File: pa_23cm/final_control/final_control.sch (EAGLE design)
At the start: 12 parts, among them IC1 MAX488CSA, IC2 7812T, IC3 7805T, J1 1X2-3.5MM

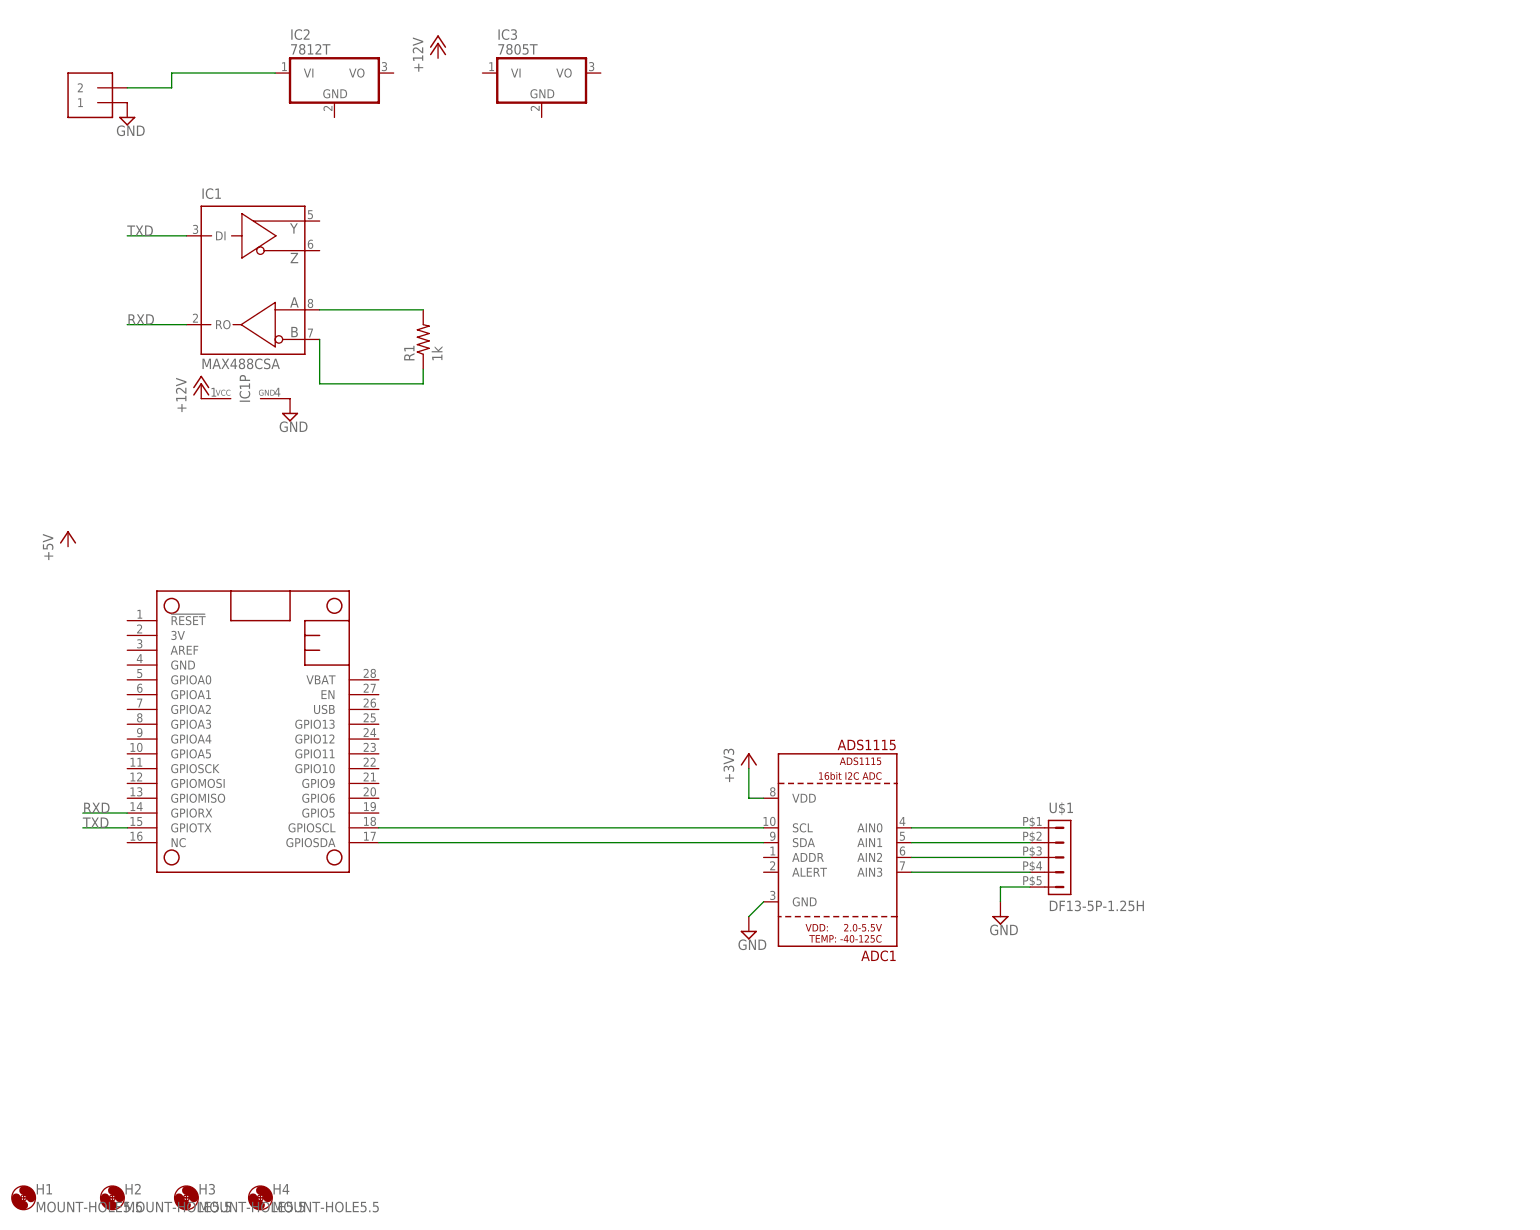
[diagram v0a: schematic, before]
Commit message: aded DECOTEC enclosure parts to library.  Updates to final control board.
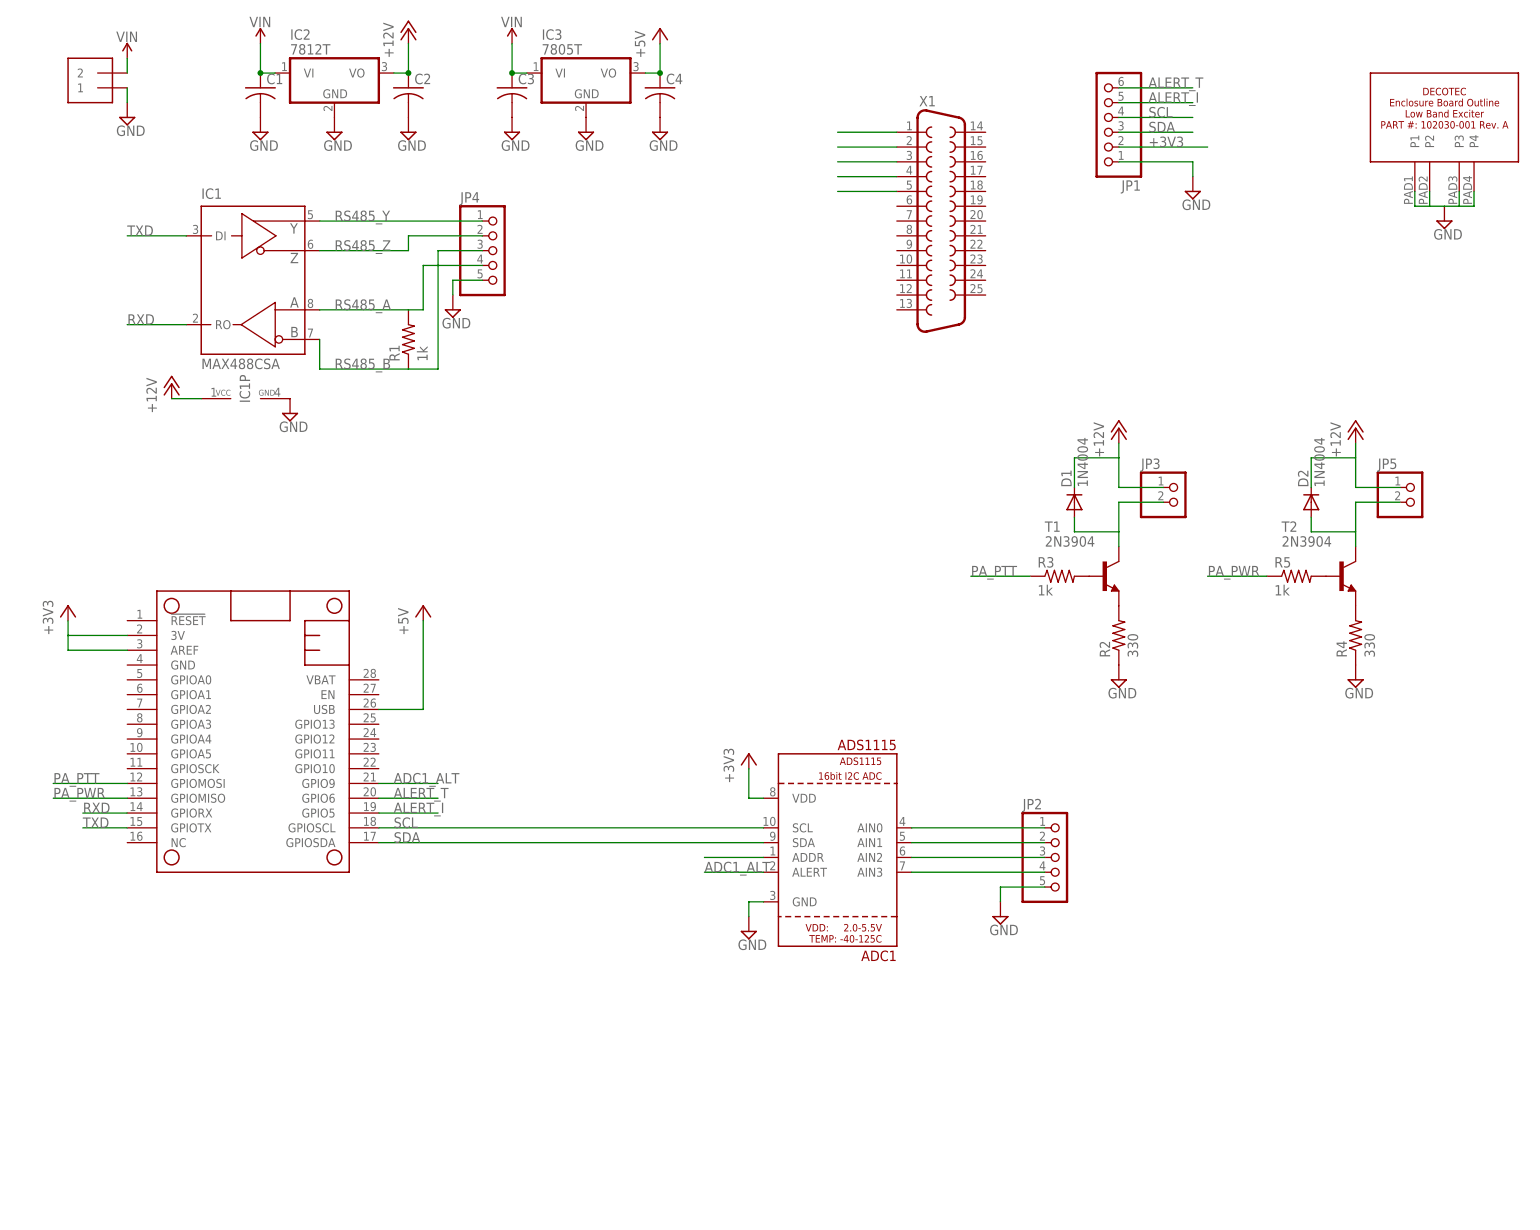
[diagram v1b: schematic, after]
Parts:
- removed H1, H2, H3, H4: MOUNT-HOLE5.5, holes:MOUNT-HOLE5.5
- removed U$1: DF13-5P-1.25H, con-hirose-df13:DF13-5P-1.25H
- added C1, C2, C3, C4: (no value), rcl:C-USC1206K
- added D1, D2: 1N4004, diode:1N4004
- added JP1: (no value), pinhead:PINHD-1X6
- added JP2, JP4: (no value), pinhead:PINHD-1X5
- added JP3, JP5: (no value), pinhead:PINHD-1X2
- added R2, R4: 330, resistor:R-US_R0805
- added R3, R5: 1k, resistor:R-US_R0805
- added T1, T2: 2N3904, transistor:2N3904
- added U$2: DECOTEC_102030-001A, vtgs:DECOTEC_102030-001A
- added X1: (no value), SparkFun-Retired:DB25_FEMALEV
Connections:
- new net +5V: C4.1, FEATHER_32U4.USB, IC3.VO
- new net ADC1_ALT: ADC1.ALERT, FEATHER_32U4.GPIO9
- new net ALERT_I: FEATHER_32U4.GPIO5, JP1.5
- new net ALERT_T: FEATHER_32U4.GPIO6, JP1.6
- new net N$10: R2.2, T1.E
- new net N$11: R3.2, T1.B
- new net N$12: X1.1
- new net N$13: X1.2
- new net N$14: X1.3
- new net N$15: X1.4
- new net N$16: X1.5
- new net PA_PTT: FEATHER_32U4.GPIOMOSI, R3.1
- new net PA_PWR: FEATHER_32U4.GPIOMISO, R5.1
- new net RS485_A: IC1G$1.A, JP4.4, R1.2
- new net RS485_B: IC1G$1.B, JP4.3, R1.1
- new net RS485_Y: IC1G$1.Y, JP4.1
- new net RS485_Z: IC1G$1.Z, JP4.2
- new net SCL: ADC1.SCL, FEATHER_32U4.GPIOSCL, JP1.4
- new net SDA: ADC1.SDA, FEATHER_32U4.GPIOSDA, JP1.3
- new net VIN: C1.1, C3.1, IC2.VI, IC3.VI, J1.2
- net +12V: now also C2.1, D1.C, D2.C, IC2.VO, JP3.1, JP5.1
- net +3V3: now also FEATHER_32U4.3V, FEATHER_32U4.AREF, JP1.2
- net GND: now also C1.2, C2.2, C3.2, C4.2, IC2.GND, IC3.GND, JP1.1, JP2.5, JP4.5, R2.1, R4.1, U$2.P1, U$2.P2, U$2.P3, U$2.P4; no longer U$1.5
- net N$1: now also ADC1.ADDR; no longer IC1G$1.A, R1.2
- net N$2: now also D2.A, JP5.2, T2.C; no longer IC1G$1.B, R1.1
- net N$3: now also R4.2, T2.E; no longer ADC1.SCL, FEATHER_32U4.GPIOSCL
- net N$4: now also R5.2, T2.B; no longer ADC1.SDA, FEATHER_32U4.GPIOSDA
- net N$5: now also JP2.1; no longer U$1.1
- net N$6: now also JP2.2; no longer U$1.2
- net N$7: now also JP2.3; no longer U$1.3
- net N$8: now also JP2.4; no longer U$1.4
- net N$9: now also D1.A, JP3.2, T1.C; no longer IC2.VI, J1.2
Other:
- moved on the sheet: IC3, R1
